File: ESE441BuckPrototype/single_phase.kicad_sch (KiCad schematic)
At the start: 8 parts

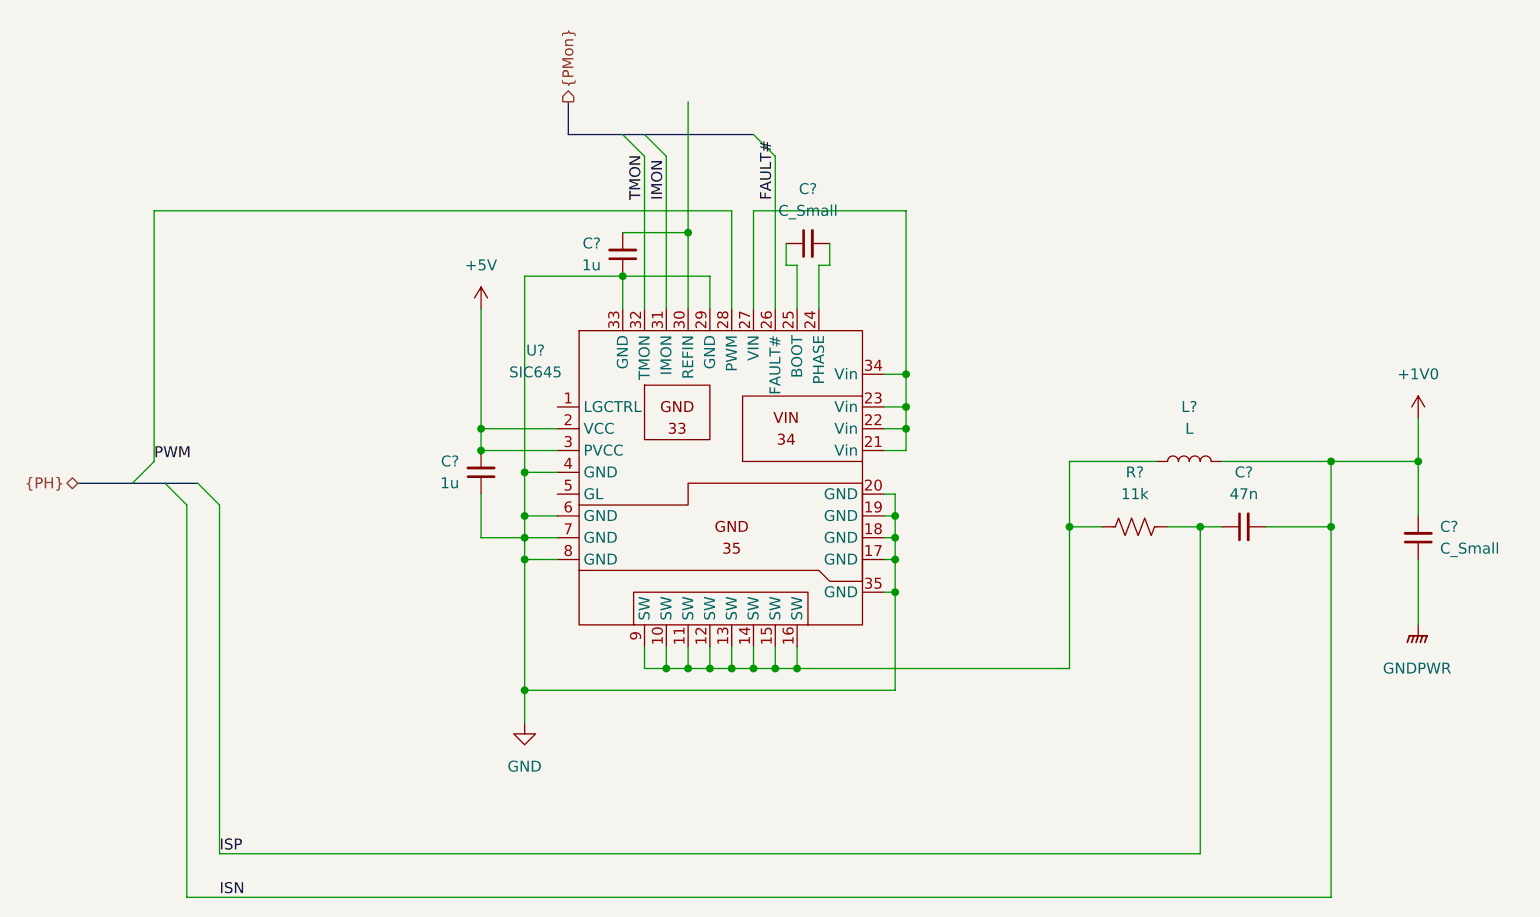
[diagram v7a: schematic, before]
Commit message: Add component names, values, PWM jumper
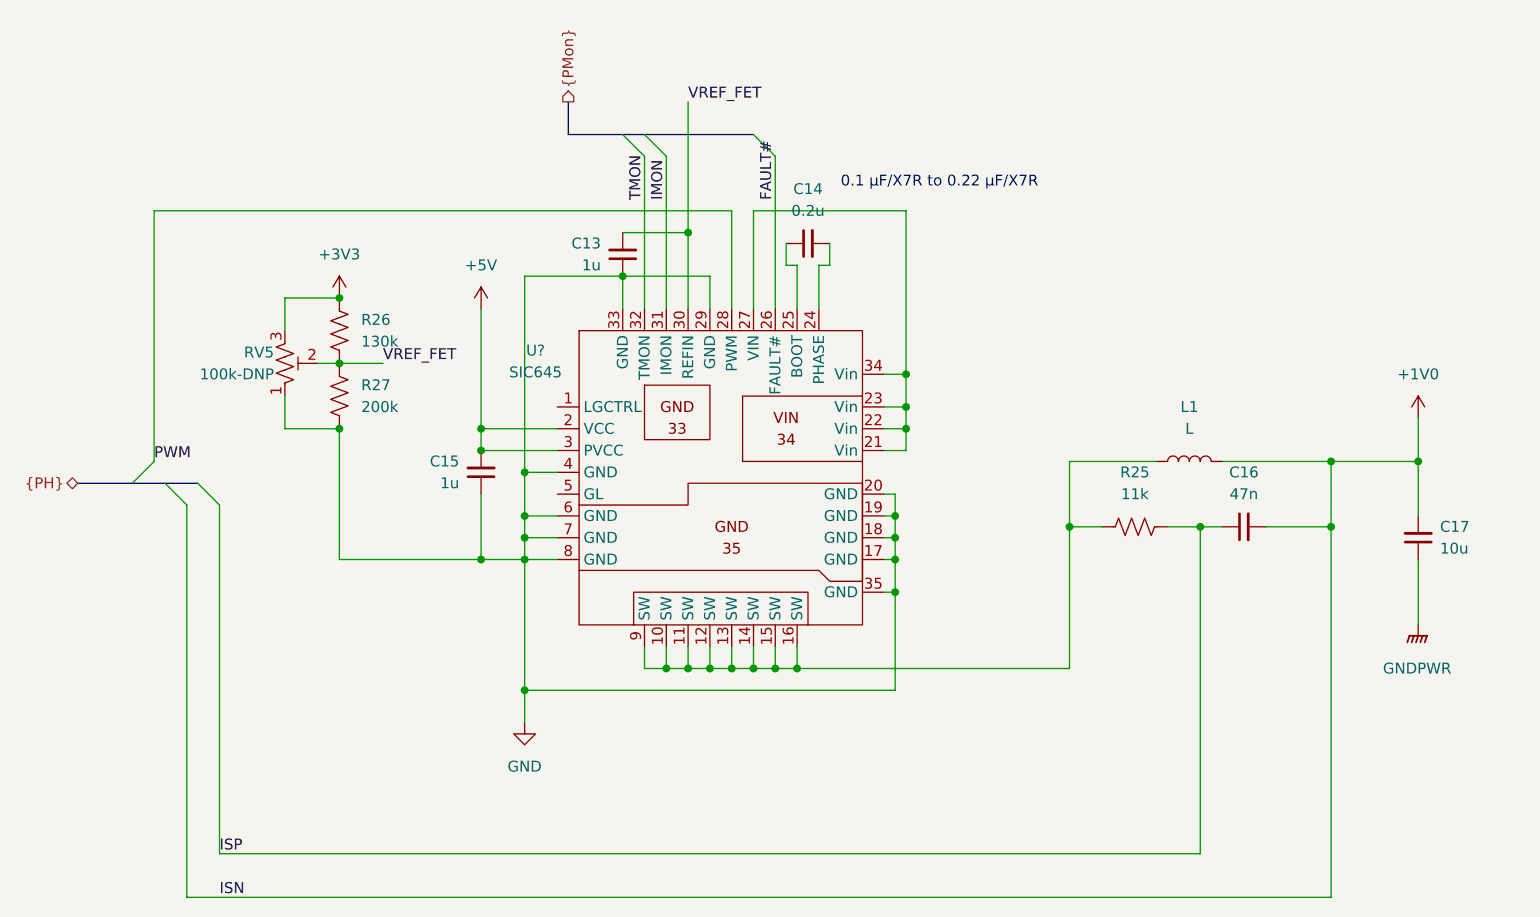
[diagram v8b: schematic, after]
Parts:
- added R26: 130k, Resistor_SMD:R_0603_1608Metric, symbol Device:R_US
- added R27: 200k, Resistor_SMD:R_0603_1608Metric, symbol Device:R_US
- added RV5: 100k-DNP, symbol Device:R_Potentiometer_Trim_US
- C14: renamed from C?; value C_Small -> 0.2u
- C16: renamed from C?; footprint (none) -> Capacitor_SMD:C_0603_1608Metric
- C17: renamed from C?; value C_Small -> 10u
- L1: renamed from L?; footprint (none) -> Inductor_SMD:L_7.3x7.3_H4.5
- R25: renamed from R?; footprint (none) -> Resistor_SMD:R_0603_1608Metric
- gave numbers to parts that had none: 2
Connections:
- net GND: now also R27.1, RV5.1
- net VREF_FET: now reaches C13.2, U?.30 (REFIN)
- net VREF_FET: now also R26.1, R27.2, RV5.2
- new net +3V3: R26.2, RV5.3
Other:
- note added: "0.1 μF/X7R to 0.22 μF/X7R"
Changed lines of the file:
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@@
   (junction (at 195.58 64.77) (diameter 0) (color 0 0 0 0)
   )
+  (junction (at 80.01 53.34) (diameter 0) (color 0 0 0 0)
+  )
   (junction (at 146.05 54.61) (diameter 0) (color 0 0 0 0)
   )
@@
   (junction (at 165.1 72.39) (diameter 0) (color 0 0 0 0)
   )
+  (junction (at 96.52 76.2) (diameter 0) (color 0 0 0 0)
+  )
   (junction (at 101.6 66.04) (diameter 0) (color 0 0 0 0)
   )
@@
   (junction (at 125.73 88.9) (diameter 0) (color 0 0 0 0)
   )
+  (junction (at 80.01 45.72) (diameter 0) (color 0 0 0 0)
+  )
   (junction (at 120.65 38.1) (diameter 0) (color 0 0 0 0)
   )
@@
   (junction (at 123.19 88.9) (diameter 0) (color 0 0 0 0)
   )
+  (junction (at 80.01 60.96) (diameter 0) (color 0 0 0 0)
+  )
   (bus_entry (at 113.03 26.67) (size 2.54 2.54)
     (stroke (width 0) (type default) (color 0 0 0 0))
@@
     (stroke (width 0) (type default) (color 0 0 0 0))
   )
-  (wire (pts (xy 96.52 73.66) (xy 101.6 73.66))
+  (wire (pts (xy 96.52 76.2) (xy 101.6 76.2))
     (stroke (width 0) (type default) (color 0 0 0 0))
   )
@@
     (stroke (width 0) (type default) (color 0 0 0 0))
   )
+  (wire (pts (xy 73.66 60.96) (xy 73.66 57.15))
+    (stroke (width 0) (type default) (color 0 0 0 0))
+  )
   (wire (pts (xy 146.05 63.5) (xy 143.51 63.5))
     (stroke (width 0) (type default) (color 0 0 0 0))
@@
     (stroke (width 0) (type default) (color 0 0 0 0))
   )
+  (wire (pts (xy 96.52 68.58) (xy 96.52 76.2))
+    (stroke (width 0) (type default) (color 0 0 0 0))
+  )
   (wire (pts (xy 144.78 91.44) (xy 101.6 91.44))
     (stroke (width 0) (type default) (color 0 0 0 0))
@@
     (stroke (width 0) (type default) (color 0 0 0 0))
   )
-  (wire (pts (xy 96.52 68.58) (xy 96.52 73.66))
+  (wire (pts (xy 96.52 76.2) (xy 80.01 76.2))
+    (stroke (width 0) (type default) (color 0 0 0 0))
+  )
+  (wire (pts (xy 73.66 45.72) (xy 73.66 49.53))
     (stroke (width 0) (type default) (color 0 0 0 0))
   )
@@
     (stroke (width 0) (type default) (color 0 0 0 0))
   )
+  (wire (pts (xy 80.01 60.96) (xy 73.66 60.96))
+    (stroke (width 0) (type default) (color 0 0 0 0))
+  )
   (wire (pts (xy 128.27 35.56) (xy 146.05 35.56))
     (stroke (width 0) (type default) (color 0 0 0 0))
@@
     (stroke (width 0) (type default) (color 0 0 0 0))
   )
+  (wire (pts (xy 80.01 45.72) (xy 73.66 45.72))
+    (stroke (width 0) (type default) (color 0 0 0 0))
+  )
   (wire (pts (xy 128.27 88.9) (xy 130.81 88.9))
     (stroke (width 0) (type default) (color 0 0 0 0))
@@
     (stroke (width 0) (type default) (color 0 0 0 0))
   )
+  (wire (pts (xy 77.47 53.34) (xy 80.01 53.34))
+    (stroke (width 0) (type default) (color 0 0 0 0))
+  )
   (wire (pts (xy 132.08 41.91) (xy 132.08 39.37))
     (stroke (width 0) (type default) (color 0 0 0 0))
@@
     (stroke (width 0) (type default) (color 0 0 0 0))
   )
+  (wire (pts (xy 80.01 53.34) (xy 85.09 53.34))
+    (stroke (width 0) (type default) (color 0 0 0 0))
+  )
   (wire (pts (xy 133.35 88.9) (xy 133.35 86.36))
     (stroke (width 0) (type default) (color 0 0 0 0))
@@
     (stroke (width 0) (type default) (color 0 0 0 0))
   )
+  (wire (pts (xy 80.01 76.2) (xy 80.01 60.96))
+    (stroke (width 0) (type default) (color 0 0 0 0))
+  )
   (wire (pts (xy 144.78 76.2) (xy 144.78 80.01))
     (stroke (width 0) (type default) (color 0 0 0 0))
@@
     (stroke (width 0) (type default) (color 0 0 0 0))
   )
+  (text "0.1 μF/X7R to 0.22 μF/X7R" (at 138.43 33.02 0)
+    (effects (font (size 1.27 1.27)) (justify left bottom))
+  )
+  (label "VREF_FET" (at 120.65 22.86 0)
+    (effects (font (size 1.27 1.27)) (justify left bottom))
+  )
   (label "FAULT#" (at 130.81 34.29 90)
     (effects (font (size 1.27 1.27)) (justify left bottom))
@@
   )
   (label "ISP" (at 66.04 110.49 0)
+    (effects (font (size 1.27 1.27)) (justify left bottom))
+  )
+  (label "VREF_FET" (at 85.09 53.34 0)
     (effects (font (size 1.27 1.27)) (justify left bottom))
   )
@@
   (symbol (lib_id "Device:C_Small") (at 205.74 73.66 180) (unit 1)
     (in_bom yes) (on_board yes) (fields_autoplaced)
-    (property "Reference" "C?" (id 0) (at 208.28 72.3835 0)
-      (effects (font (size 1.27 1.27)) (justify right))
-    )
-    (property "Value" "C_Small" (id 1) (at 208.28 74.9235 0)
+    (property "Reference" "C17" (id 0) (at 208.28 72.3835 0)
+      (effects (font (size 1.27 1.27)) (justify right))
+    )
+    (property "Value" "10u" (id 1) (at 208.28 74.9235 0)
       (effects (font (size 1.27 1.27)) (justify right))
     )
@@
   (symbol (lib_id "Device:R_US") (at 172.72 72.39 90) (unit 1)
     (in_bom yes) (on_board yes) (fields_autoplaced)
-    (property "Reference" "R?" (id 0) (at 172.72 66.04 90))
+    (property "Reference" "R25" (id 0) (at 172.72 66.04 90))
     (property "Value" "11k" (id 1) (at 172.72 68.58 90))
-    (property "Footprint" "" (id 2) (at 172.974 71.374 90)
+    (property "Footprint" "Resistor_SMD:R_0603_1608Metric" (id 2) (at 172.974 71.374 90)
       (effects (font (size 1.27 1.27)) hide)
     )
@@
     (pin "2")
   )
+  (symbol (lib_id "Device:R_Potentiometer_Trim_US") (at 73.66 53.34 0) (mirror x) (unit 1)
+    (in_bom yes) (on_board yes)
+    (property "Reference" "RV5" (id 0) (at 72.39 52.0699 0)
+      (effects (font (size 1.27 1.27)) (justify right))
+    )
+    (property "Value" "100k-DNP" (id 1) (at 72.39 54.6099 0)
+      (effects (font (size 1.27 1.27)) (justify right))
+    )
+    (property "Footprint" "" (id 2) (at 73.66 53.34 0)
+      (effects (font (size 1.27 1.27)) hide)
+    )
+    (property "Datasheet" "~" (id 3) (at 73.66 53.34 0)
+      (effects (font (size 1.27 1.27)) hide)
+    )
+    (pin "1")
+    (pin "2")
+    (pin "3")
+  )
   (symbol (lib_id "Device:L") (at 179.07 64.77 90) (unit 1)
     (in_bom yes) (on_board yes) (fields_autoplaced)
-    (property "Reference" "L?" (id 0) (at 179.07 58.42 90))
+    (property "Reference" "L1" (id 0) (at 179.07 58.42 90))
     (property "Value" "L" (id 1) (at 179.07 60.96 90))
-    (property "Footprint" "" (id 2) (at 179.07 64.77 0)
+    (property "Footprint" "Inductor_SMD:L_7.3x7.3_H4.5" (id 2) (at 179.07 64.77 0)
       (effects (font (size 1.27 1.27)) hide)
     )
@@
   (symbol (lib_id "Device:C_Small") (at 134.62 39.37 90) (unit 1)
     (in_bom yes) (on_board yes)
-    (property "Reference" "C?" (id 0) (at 134.6263 33.02 90))
-    (property "Value" "C_Small" (id 1) (at 134.6263 35.56 90))
+    (property "Reference" "C14" (id 0) (at 134.6263 33.02 90))
+    (property "Value" "0.2u" (id 1) (at 134.6263 35.56 90))
     (property "Footprint" "Capacitor_SMD:C_0603_1608Metric" (id 2) (at 134.62 39.37 0)
       (effects (font (size 1.27 1.27)) hide)
@@
     (pin "2")
   )
+  (symbol (lib_id "power:+3V3") (at 80.01 45.72 0) (unit 1)
+    (in_bom yes) (on_board yes) (fields_autoplaced)
+    (property "Reference" "#PWR?" (id 0) (at 80.01 49.53 0)
+      (effects (font (size 1.27 1.27)) hide)
+    )
+    (property "Value" "+3V3" (id 1) (at 80.01 40.64 0))
+    (property "Footprint" "" (id 2) (at 80.01 45.72 0)
+      (effects (font (size 1.27 1.27)) hide)
+    )
+    (property "Datasheet" "" (id 3) (at 80.01 45.72 0)
+      (effects (font (size 1.27 1.27)) hide)
+    )
+    (pin "1")
+  )
+  (symbol (lib_id "Device:R_US") (at 80.01 49.53 180) (unit 1)
+    (in_bom yes) (on_board yes) (fields_autoplaced)
+    (property "Reference" "R26" (id 0) (at 82.55 48.2599 0)
+      (effects (font (size 1.27 1.27)) (justify right))
+    )
+    (property "Value" "130k" (id 1) (at 82.55 50.7999 0)
+      (effects (font (size 1.27 1.27)) (justify right))
+    )
+    (property "Footprint" "Resistor_SMD:R_0603_1608Metric" (id 2) (at 78.994 49.276 90)
+      (effects (font (size 1.27 1.27)) hide)
+    )
+    (property "Datasheet" "~" (id 3) (at 80.01 49.53 0)
+      (effects (font (size 1.27 1.27)) hide)
+    )
+    (pin "1")
+    (pin "2")
+  )
   (symbol (lib_id "Device:C_Small") (at 185.42 72.39 90) (unit 1)
     (in_bom yes) (on_board yes) (fields_autoplaced)
-    (property "Reference" "C?" (id 0) (at 185.4263 66.04 90))
+    (property "Reference" "C16" (id 0) (at 185.4263 66.04 90))
     (property "Value" "47n" (id 1) (at 185.4263 68.58 90))
-    (property "Footprint" "" (id 2) (at 185.42 72.39 0)
+    (property "Footprint" "Capacitor_SMD:C_0603_1608Metric" (id 2) (at 185.42 72.39 0)
       (effects (font (size 1.27 1.27)) hide)
     )
@@
     )
     (pin "1")
+  )
+  (symbol (lib_id "Device:R_US") (at 80.01 57.15 180) (unit 1)
+    (in_bom yes) (on_board yes) (fields_autoplaced)
+    (property "Reference" "R27" (id 0) (at 82.55 55.8799 0)
+      (effects (font (size 1.27 1.27)) (justify right))
+    )
+    (property "Value" "200k" (id 1) (at 82.55 58.4199 0)
+      (effects (font (size 1.27 1.27)) (justify right))
+    )
+    (property "Footprint" "Resistor_SMD:R_0603_1608Metric" (id 2) (at 78.994 56.896 90)
+      (effects (font (size 1.27 1.27)) hide)
+    )
+    (property "Datasheet" "~" (id 3) (at 80.01 57.15 0)
+      (effects (font (size 1.27 1.27)) hide)
+    )
+    (pin "1")
+    (pin "2")
   )
   (symbol (lib_id "CustomPartsLibrary:SIC645") (at 124.46 67.31 0) (unit 1)
@@
   (symbol (lib_id "Device:C_Small") (at 113.03 40.64 0) (mirror x) (unit 1)
     (in_bom yes) (on_board yes) (fields_autoplaced)
-    (property "Reference" "C?" (id 0) (at 110.49 39.3635 0)
+    (property "Reference" "C13" (id 0) (at 110.49 39.3635 0)
       (effects (font (size 1.27 1.27)) (justify right))
     )
@@
   (symbol (lib_id "Device:C_Small") (at 96.52 66.04 0) (mirror x) (unit 1)
     (in_bom yes) (on_board yes) (fields_autoplaced)
-    (property "Reference" "C?" (id 0) (at 93.98 64.7635 0)
-      (effects (font (size 1.27 1.27)) (justify right))
-    )
+    (property "Reference" "C15" (id 0) (at 93.98 64.7635 0)
+      (effects (font (size 1.27 1.27)) (justify right))
+    )
